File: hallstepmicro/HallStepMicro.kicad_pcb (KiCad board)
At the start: 2 copper layers, 30.5 x 55.9 mm, 26 parts, among them IC1 ATTINY84A-SS

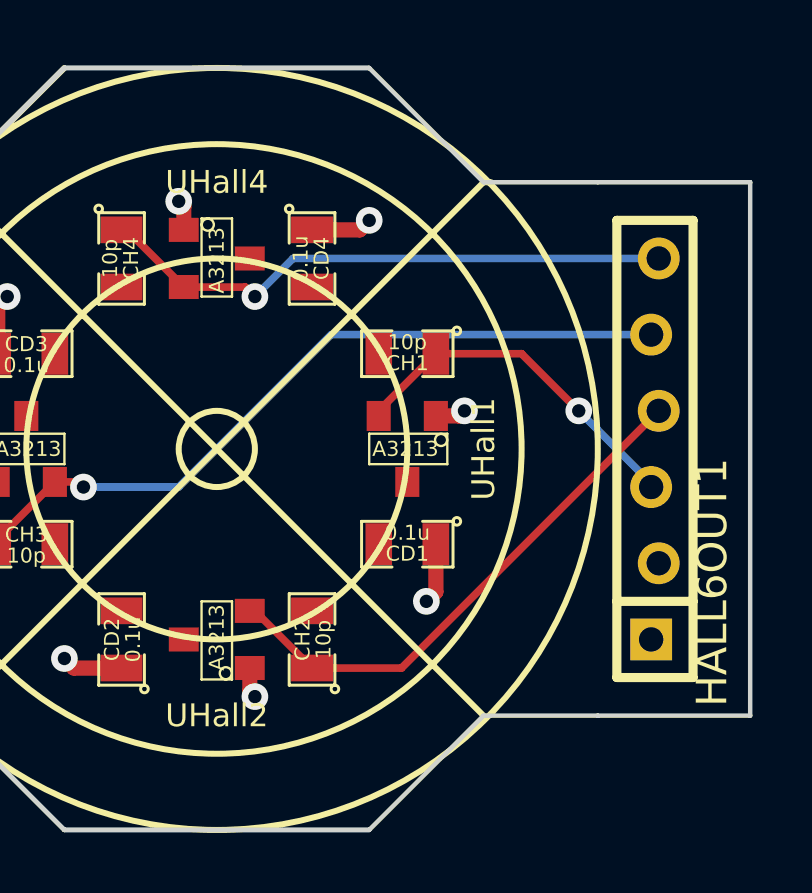
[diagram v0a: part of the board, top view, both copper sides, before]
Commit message: Shrinking sensor mount
Shrinking sensor mount dimensions. Intermediate checkin before
repositioning connector.
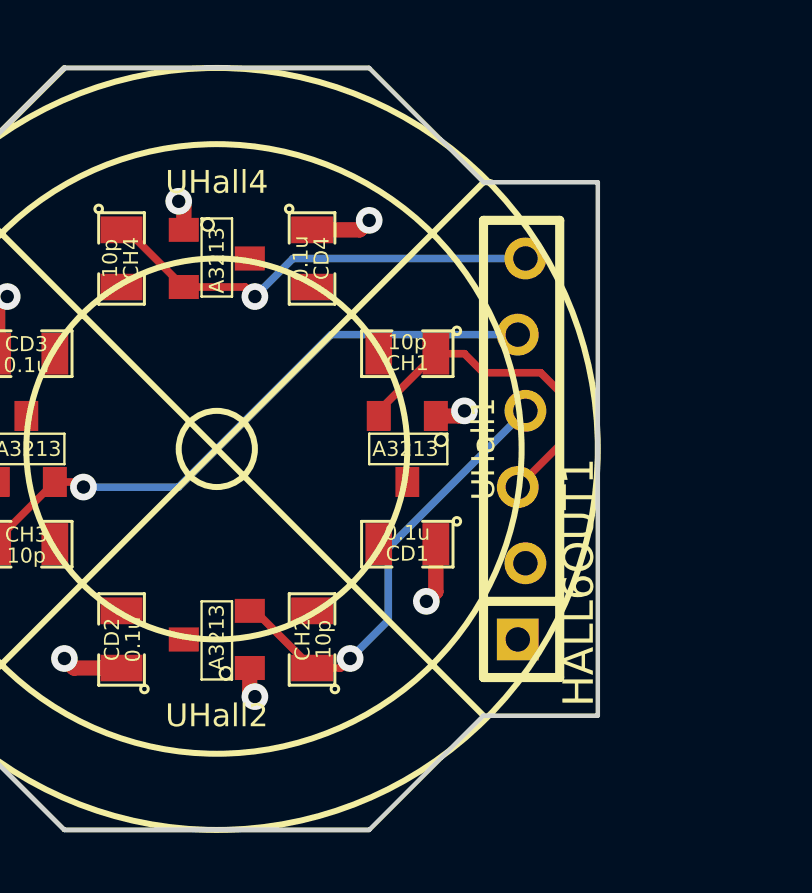
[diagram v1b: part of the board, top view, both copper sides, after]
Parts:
- moved HALL6OUT1 4.44 mm to (137.2, 76.2)
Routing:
- net /HallSensors1/hall3: track 24.9 -> 20.5 mm
- net /HallSensors1/hall4: track 19.7 -> 15.3 mm
- net /HallSensors1/hall2: track 18.0 -> 14.9 mm, vias 0 -> 1
- net /HallSensors1/hall1: track 12.0 -> 11.3 mm, vias 1 -> 0
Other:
- board size 30.5 x 55.9 mm -> 25.4 x 55.9 mm
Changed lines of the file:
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@@
-(kicad_pcb (version 3) (host pcbnew "(2013-mar-25)-stable")
+(kicad_pcb (version 3) (host pcbnew "(2013-07-07 BZR 4022)-stable")
   (general
     (links 70)
     (no_connects 0)
-    (area 101.229524 26.500001 144.855001 94.075)
+    (area 103.769524 26.500001 144.855001 94.075)
     (thickness 1.6)
-    (drawings 36)
-    (tracks 146)
+    (drawings 34)
+    (tracks 151)
     (zones 0)
     (modules 26)
@@
       (usegerberextensions true)
       (excludeedgelayer true)
-      (linewidth 0)
+      (linewidth 0.150000)
       (plotframeref false)
       (viasonmask false)
@@
   )
   (module SIL6-offset-0p005 (layer F.Cu)
-    (at 141.605 76.2 90)
+    (at 137.16 76.2 90)
     (descr "Connecteur 6 pins")
     (tags "CONN DEV")
@@
     )
   )
+  (gr_line (start 139.7 67.31) (end 139.7 85.09) (angle 90) (layer Edge.Cuts) (width 0.15))
   (gr_line (start 114.3 33.02) (end 139.7 33.02) (angle 90) (layer Edge.Cuts) (width 0.15))
   (gr_line (start 139.7 58.42) (end 114.3 58.42) (angle 90) (layer Edge.Cuts) (width 0.15))
@@
     (arrow2b (pts (xy 108.585 58.42) (xy 107.99858 57.293497)))
   )
-  (gr_line (start 144.78 67.31) (end 139.7 67.31) (angle 90) (layer Edge.Cuts) (width 0.15))
-  (gr_line (start 144.78 85.09) (end 144.78 67.31) (angle 90) (layer Edge.Cuts) (width 0.15))
-  (gr_line (start 139.7 85.09) (end 144.78 85.09) (angle 90) (layer Edge.Cuts) (width 0.15))
   (dimension 30.48 (width 0.25) (layer F.SilkS)
     (gr_text "1.2000 in" (at 129.54 93.074999) (layer F.SilkS)
@@
   (segment (start 133.6675 48.26) (end 133.6675 50.8) (width 0.254) (layer F.Cu) (net 4))
   (segment (start 133.6675 48.26) (end 135.89 48.26) (width 0.254) (layer F.Cu) (net 4))
-  (segment (start 134.3025 73.025) (end 137.16 73.025) (width 0.254) (layer F.Cu) (net 5))
-  (segment (start 141.478 77.343) (end 141.478 77.47) (width 0.254) (layer B.Cu) (net 5))
-  (segment (start 139.065 74.93) (end 141.478 77.343) (width 0.254) (layer B.Cu) (net 5))
-  (via (at 139.065 74.93) (size 0.889) (layers F.Cu B.Cu) (net 5))
-  (segment (start 137.16 73.025) (end 139.065 74.93) (width 0.254) (layer F.Cu) (net 5))
+  (segment (start 134.3025 73.025) (end 135.255 73.025) (width 0.254) (layer F.Cu) (net 5))
+  (segment (start 138.43 76.073) (end 137.033 77.47) (width 0.254) (layer F.Cu) (net 5))
+  (segment (start 138.43 74.295) (end 138.43 76.073) (width 0.254) (layer F.Cu) (net 5))
+  (segment (start 137.795 73.66) (end 138.43 74.295) (width 0.254) (layer F.Cu) (net 5))
+  (segment (start 135.89 73.66) (end 137.795 73.66) (width 0.254) (layer F.Cu) (net 5))
+  (segment (start 135.255 73.025) (end 135.89 73.66) (width 0.254) (layer F.Cu) (net 5))
   (segment (start 132.3975 75.10018) (end 132.3975 74.93) (width 0.254) (layer F.Cu) (net 5))
   (segment (start 132.3975 74.93) (end 134.3025 73.025) (width 0.254) (layer F.Cu) (net 5))
-  (segment (start 130.175 83.5025) (end 133.1595 83.5025) (width 0.254) (layer F.Cu) (net 6))
-  (segment (start 133.1595 83.5025) (end 141.732 74.93) (width 0.254) (layer F.Cu) (net 6))
+  (segment (start 130.175 83.5025) (end 131.1275 83.5025) (width 0.254) (layer F.Cu) (net 6))
+  (segment (start 132.715 79.502) (end 137.287 74.93) (width 0.254) (layer B.Cu) (net 6))
+  (segment (start 132.715 81.915) (end 132.715 79.502) (width 0.254) (layer B.Cu) (net 6))
+  (segment (start 131.445 83.185) (end 132.715 81.915) (width 0.254) (layer B.Cu) (net 6))
+  (via (at 131.445 83.185) (size 0.889) (layers F.Cu B.Cu) (net 6))
+  (segment (start 131.1275 83.5025) (end 131.445 83.185) (width 0.254) (layer F.Cu) (net 6))
   (segment (start 128.09982 81.5975) (end 128.27 81.5975) (width 0.254) (layer F.Cu) (net 6))
   (segment (start 128.27 81.5975) (end 130.175 83.5025) (width 0.254) (layer F.Cu) (net 6))
-  (segment (start 141.478 72.39) (end 130.81 72.39) (width 0.254) (layer B.Cu) (net 7))
+  (segment (start 137.033 72.39) (end 130.81 72.39) (width 0.254) (layer B.Cu) (net 7))
   (segment (start 122.38482 77.29982) (end 121.6025 77.29982) (width 0.254) (layer F.Cu) (net 7))
   (segment (start 122.555 77.47) (end 122.38482 77.29982) (width 0.254) (layer F.Cu) (net 7))
@@
   (segment (start 119.6975 79.375) (end 119.6975 79.20482) (width 0.254) (layer F.Cu) (net 7))
   (segment (start 119.6975 79.20482) (end 121.6025 77.29982) (width 0.254) (layer F.Cu) (net 7))
-  (segment (start 125.90018 70.8025) (end 127.9525 70.8025) (width 0.254) (layer F.Cu) (net 8))
-  (segment (start 129.54 69.85) (end 141.732 69.85) (width 0.254) (layer B.Cu) (net 8))
+  (segment (start 137.287 69.85) (end 129.54 69.85) (width 0.254) (layer B.Cu) (net 8))
+  (segment (start 127.9525 70.8025) (end 125.90018 70.8025) (width 0.254) (layer F.Cu) (net 8))
   (segment (start 128.27 71.12) (end 129.54 69.85) (width 0.254) (layer B.Cu) (net 8))
   (via (at 128.27 71.12) (size 0.889) (layers F.Cu B.Cu) (net 8))
@@
     (polygon
       (pts
-        (xy 144.78 85.09) (xy 135.89 85.09) (xy 132.08 88.9) (xy 121.92 88.9) (xy 114.3 81.28)
-        (xy 114.3 71.12) (xy 121.92 63.5) (xy 132.08 63.5) (xy 135.89 67.31) (xy 144.78 67.31)
+        (xy 139.7 85.09) (xy 135.89 85.09) (xy 132.08 88.9) (xy 121.92 88.9) (xy 114.3 81.28)
+        (xy 114.3 71.12) (xy 121.92 63.5) (xy 132.08 63.5) (xy 135.89 67.31) (xy 139.7 67.31)
       )
     )
@@
     (polygon
       (pts
-        (xy 144.78 85.09) (xy 135.89 85.09) (xy 132.08 88.9) (xy 121.92 88.9) (xy 114.3 81.28)
-        (xy 114.3 71.12) (xy 121.92 63.5) (xy 132.08 63.5) (xy 135.89 67.31) (xy 144.78 67.31)
+        (xy 139.7 85.09) (xy 135.89 85.09) (xy 132.08 88.9) (xy 121.92 88.9) (xy 114.3 81.28)
+        (xy 114.3 71.12) (xy 121.92 63.5) (xy 132.08 63.5) (xy 135.89 67.31) (xy 139.7 67.31)
       )
     )

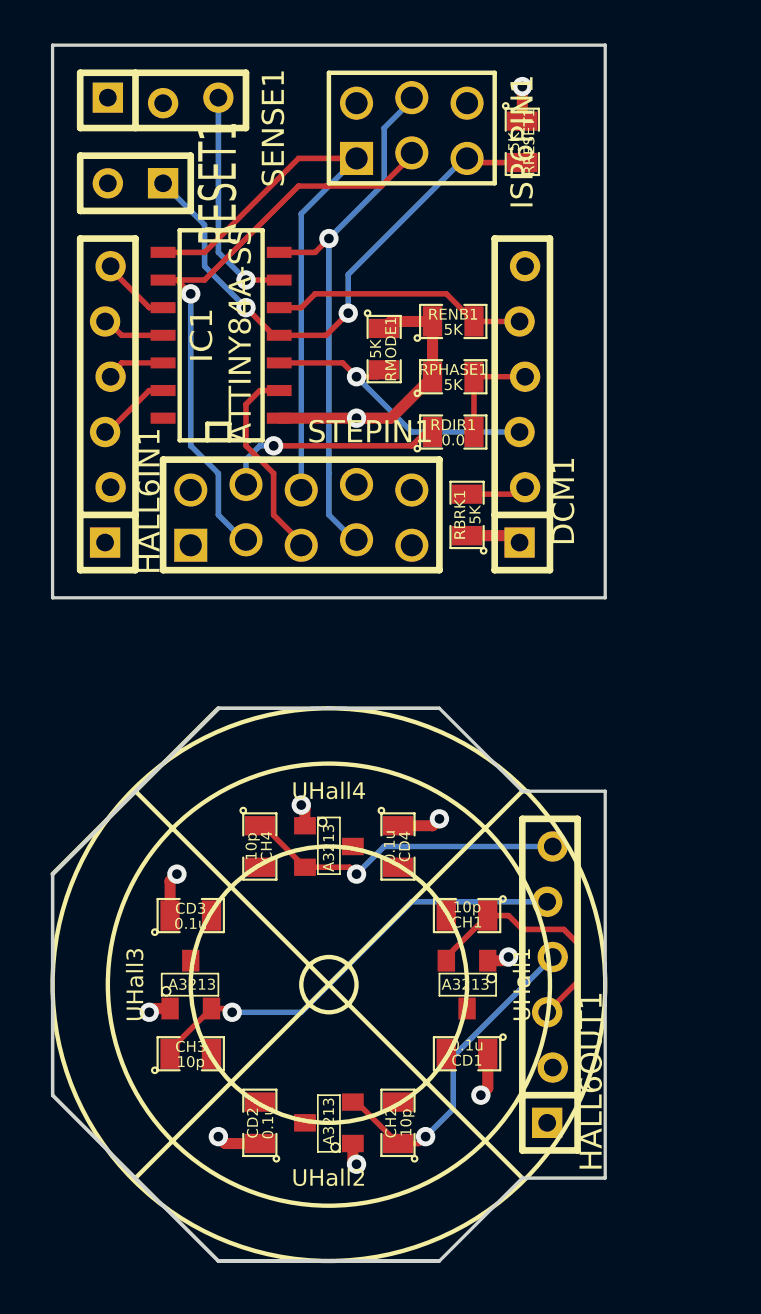
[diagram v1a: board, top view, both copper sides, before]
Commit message: Cleaned up routing.
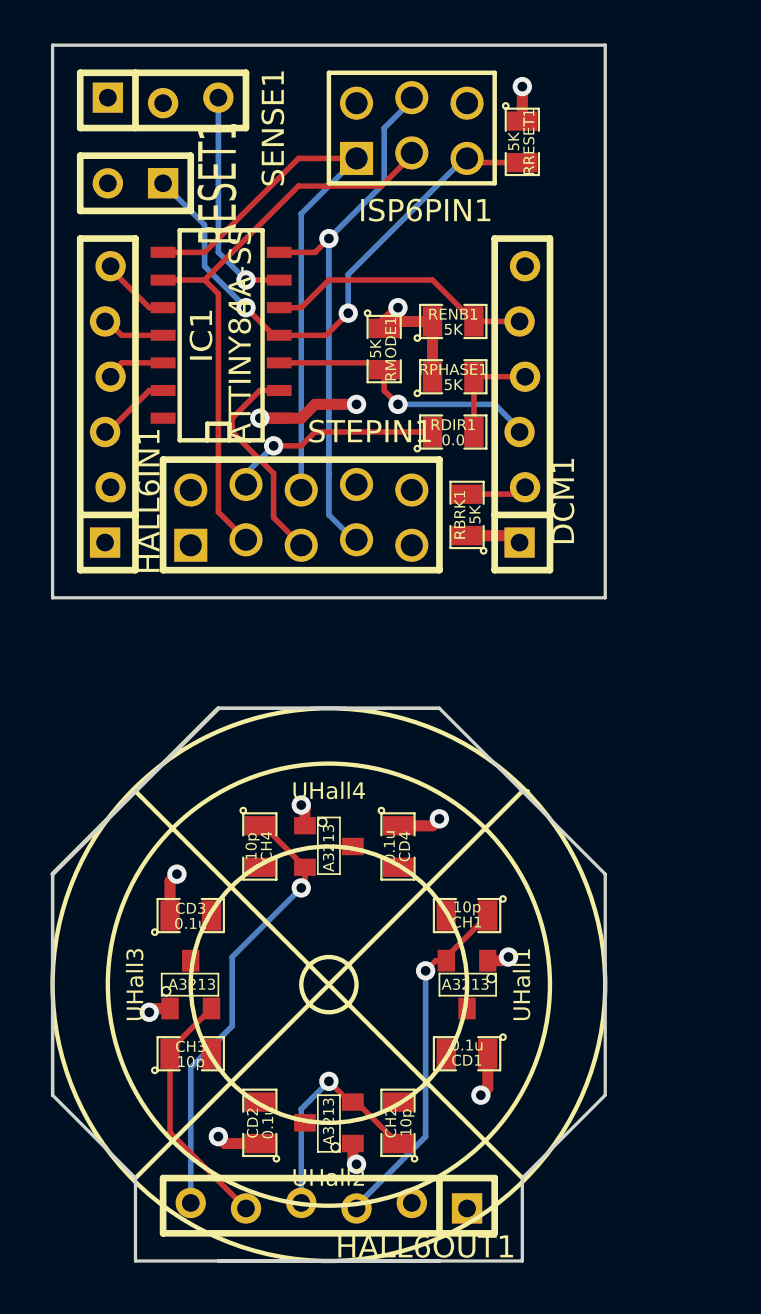
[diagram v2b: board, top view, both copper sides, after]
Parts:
- moved HALL6OUT1 14.4 mm to (127.0, 86.4), turned to 180 degrees
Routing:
- net /HallSensors1/hall3: track 20.5 -> 11.4 mm, vias 1 -> 0
- net /HallSensors1/hall4: track 15.3 -> 20.8 mm
- net /HallSensors1/hall1: track 11.3 -> 16.2 mm, vias 0 -> 1
- net /HallSensors1/hall2: track 14.9 -> 10.5 mm
- net VDD: track 17.0 -> 15.1 mm, vias 2 -> 4
- net /DC_MODE: track 14.5 -> 13.0 mm
- net /STP_STEP: track 27.8 -> 27.2 mm, vias 1 -> 0
- net /STP_ENB: track 9.19 -> 9.84 mm
- net /DC_ENABLE: track 12.0 -> 12.5 mm
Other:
- outline, holes or cut-outs redrawn

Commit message: Misc clean-up. Considered adding back TO92 case option but made design too cluttered.
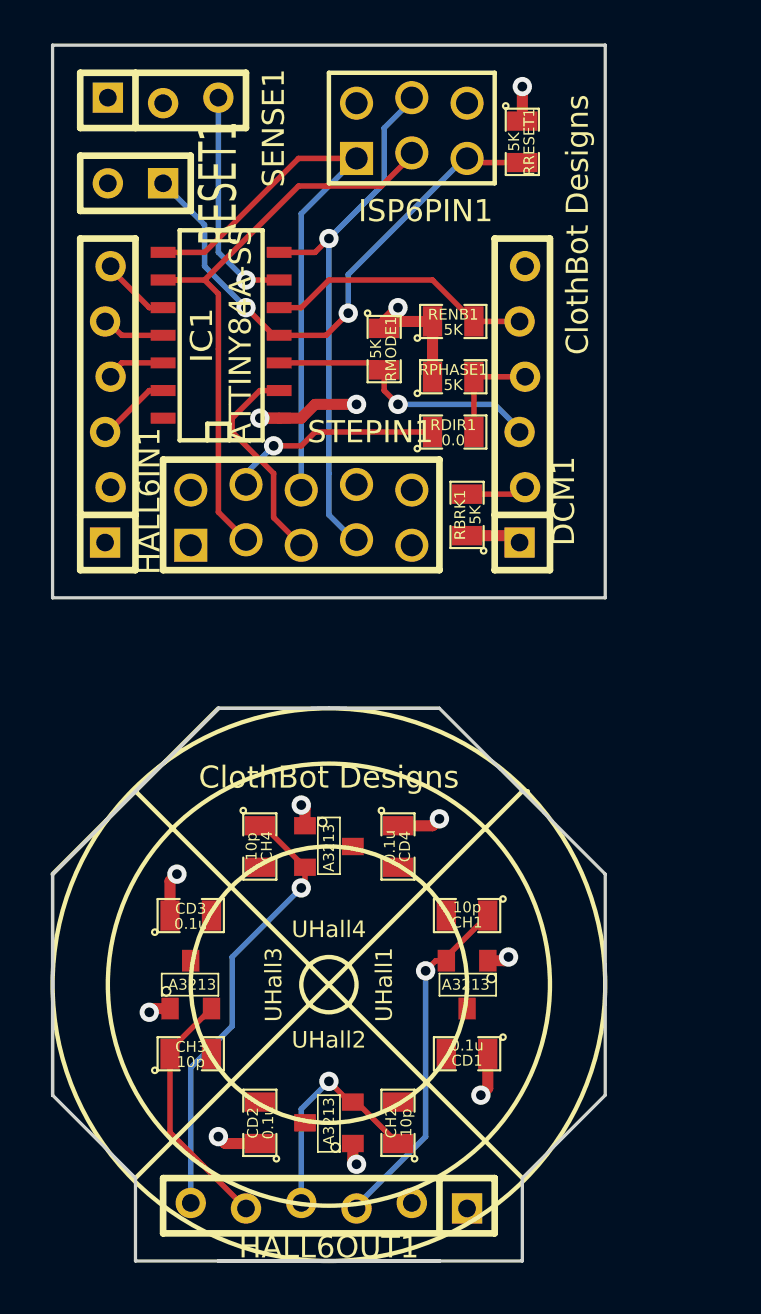
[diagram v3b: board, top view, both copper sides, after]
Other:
- board text added: "ClothBot Designs"
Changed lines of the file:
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@@
-(kicad_pcb (version 3) (host pcbnew "(2013-07-07 BZR 4022)-stable")
+(kicad_pcb (version 3) (host pcbnew "(2013-mar-25)-stable")
   (general
     (links 70)
     (no_connects 0)
-    (area 103.769524 26.500001 144.780001 94.075)
+    (area 98.171 26.500001 151.536401 100.736401)
     (thickness 1.6)
-    (drawings 35)
+    (drawings 33)
     (tracks 149)
     (zones 0)
@@
       (usegerberextensions true)
       (excludeedgelayer true)
-      (linewidth 0.150000)
+      (linewidth 0)
       (plotframeref false)
       (viasonmask false)
@@
       (effects (font (size 1.72974 1.08712) (thickness 0.3048)))
     )
-    (fp_text value CONN_2 (at 6.35 2.54 180) (layer F.SilkS) hide
+    (fp_text value CONN_2 (at 0 0 180) (layer F.SilkS) hide
       (effects (font (size 1.524 1.016) (thickness 0.3048)))
     )
@@
     (tags SOT23)
     (attr smd)
-    (fp_text reference UHall4 (at -2.54 0 360) (layer F.SilkS)
+    (fp_text reference UHall4 (at 3.81 0 360) (layer F.SilkS)
       (effects (font (size 0.762 0.762) (thickness 0.11938)))
     )
@@
     (tags SOT23)
     (attr smd)
-    (fp_text reference UHall3 (at -2.54 0 90) (layer F.SilkS)
+    (fp_text reference UHall3 (at 3.81 0 90) (layer F.SilkS)
       (effects (font (size 0.762 0.762) (thickness 0.11938)))
     )
@@
     (tags SOT23)
     (attr smd)
-    (fp_text reference UHall2 (at -2.54 0 180) (layer F.SilkS)
+    (fp_text reference UHall2 (at 3.81 0 180) (layer F.SilkS)
       (effects (font (size 0.762 0.762) (thickness 0.11938)))
     )
@@
     (tags SOT23)
     (attr smd)
-    (fp_text reference UHall1 (at -2.54 0 270) (layer F.SilkS)
+    (fp_text reference UHall1 (at 3.81 0 270) (layer F.SilkS)
       (effects (font (size 0.762 0.762) (thickness 0.11938)))
     )
@@
     (descr "Connecteur 6 pins")
     (tags "CONN DEV")
-    (fp_text reference HALL6OUT1 (at -4.445 -1.905 180) (layer F.SilkS)
-      (effects (font (size 1.016 1.016) (thickness 0.2032)))
-    )
-    (fp_text value CONN_6 (at 5.08 -2.54 180) (layer F.SilkS) hide
+    (fp_text reference HALL6OUT1 (at 0 -1.905 180) (layer F.SilkS)
+      (effects (font (size 1.016 1.016) (thickness 0.2032)))
+    )
+    (fp_text value CONN_6 (at 3.81 0 180) (layer F.SilkS) hide
       (effects (font (size 1.016 1.016) (thickness 0.2032)))
     )
@@
       (effects (font (size 1.016 1.016) (thickness 0.2032)))
     )
-    (fp_text value CONN_6 (at 5.08 -2.54 90) (layer F.SilkS) hide
+    (fp_text value CONN_6 (at 5.08 -1.27 90) (layer F.SilkS) hide
       (effects (font (size 1.016 1.016) (thickness 0.2032)))
     )
@@
       (effects (font (size 1.016 1.016) (thickness 0.2032)))
     )
-    (fp_text value CONN_3 (at 0 -1.905) (layer F.SilkS) hide
+    (fp_text value CONN_3 (at 0 0) (layer F.SilkS) hide
       (effects (font (size 1.016 1.016) (thickness 0.2032)))
     )
@@
       (effects (font (size 1.016 1.016) (thickness 0.2032)))
     )
-    (fp_text value CONN_5X2 (at -3.81 3.81) (layer F.SilkS) hide
+    (fp_text value CONN_5X2 (at -1.27 0) (layer F.SilkS) hide
       (effects (font (size 1.016 1.016) (thickness 0.2032)))
     )
@@
     )
   )
-  (dimension 25.4 (width 0.25) (layer F.SilkS)
-    (gr_text "1.0000 in" (at 127 92.439999) (layer F.SilkS)
-      (effects (font (size 1 1) (thickness 0.25)))
-    )
-    (feature1 (pts (xy 139.7 76.2) (xy 139.7 93.439999)))
-    (feature2 (pts (xy 114.3 76.2) (xy 114.3 93.439999)))
-    (crossbar (pts (xy 114.3 91.439999) (xy 139.7 91.439999)))
-    (arrow1a (pts (xy 139.7 91.439999) (xy 138.573497 92.026419)))
-    (arrow1b (pts (xy 139.7 91.439999) (xy 138.573497 90.853579)))
-    (arrow2a (pts (xy 114.3 91.439999) (xy 115.426503 92.026419)))
-    (arrow2b (pts (xy 114.3 91.439999) (xy 115.426503 90.853579)))
+  (gr_text "ClothBot Designs" (at 138.43 41.275 90) (layer F.SilkS)
+    (effects (font (size 1.016 1.016) (thickness 0.2032)))
+  )
+  (gr_text "ClothBot Designs" (at 127 66.675) (layer F.SilkS)
+    (effects (font (size 1.016 1.016) (thickness 0.2032)))
   )
   (gr_line (start 114.3 81.28) (end 118.11 85.09) (angle 90) (layer Edge.Cuts) (width 0.15))
@@
   (gr_line (start 139.7 58.42) (end 114.3 58.42) (angle 90) (layer Edge.Cuts) (width 0.15))
   (gr_line (start 139.7 33.02) (end 139.7 58.42) (angle 90) (layer Edge.Cuts) (width 0.15))
-  (dimension 25.4 (width 0.25) (layer F.SilkS)
-    (gr_text "1.0000 in" (at 127 27.575001) (layer F.SilkS)
-      (effects (font (size 1 1) (thickness 0.25)))
-    )
-    (feature1 (pts (xy 139.7 33.02) (xy 139.7 26.575001)))
-    (feature2 (pts (xy 114.3 33.02) (xy 114.3 26.575001)))
-    (crossbar (pts (xy 114.3 28.575001) (xy 139.7 28.575001)))
-    (arrow1a (pts (xy 139.7 28.575001) (xy 138.573497 29.161421)))
-    (arrow1b (pts (xy 139.7 28.575001) (xy 138.573497 27.988581)))
-    (arrow2a (pts (xy 114.3 28.575001) (xy 115.426503 29.161421)))
-    (arrow2b (pts (xy 114.3 28.575001) (xy 115.426503 27.988581)))
-  )
-  (dimension 25.4 (width 0.25) (layer F.SilkS)
-    (gr_text "1.0000 in" (at 107.585 45.72 90) (layer F.SilkS)
-      (effects (font (size 1 1) (thickness 0.25)))
-    )
-    (feature1 (pts (xy 114.3 33.02) (xy 106.585 33.02)))
-    (feature2 (pts (xy 114.3 58.42) (xy 106.585 58.42)))
-    (crossbar (pts (xy 108.585 58.42) (xy 108.585 33.02)))
-    (arrow1a (pts (xy 108.585 33.02) (xy 109.17142 34.146503)))
-    (arrow1b (pts (xy 108.585 33.02) (xy 107.99858 34.146503)))
-    (arrow2a (pts (xy 108.585 58.42) (xy 109.17142 57.293497)))
-    (arrow2b (pts (xy 108.585 58.42) (xy 107.99858 57.293497)))
-  )
-  (dimension 25.4 (width 0.25) (layer F.SilkS)
-    (gr_text "1.0000 in" (at 110.506 76.2 90) (layer F.SilkS)
-      (effects (font (size 1 1) (thickness 0.25)))
-    )
-    (feature1 (pts (xy 121.92 63.5) (xy 109.506 63.5)))
-    (feature2 (pts (xy 121.92 88.9) (xy 109.506 88.9)))
-    (crossbar (pts (xy 111.506 88.9) (xy 111.506 63.5)))
-    (arrow1a (pts (xy 111.506 63.5) (xy 112.09242 64.626503)))
-    (arrow1b (pts (xy 111.506 63.5) (xy 110.91958 64.626503)))
-    (arrow2a (pts (xy 111.506 88.9) (xy 112.09242 87.773497)))
-    (arrow2b (pts (xy 111.506 88.9) (xy 110.91958 87.773497)))
-  )
   (gr_line (start 114.3 58.42) (end 114.3 33.02) (angle 90) (layer Edge.Cuts) (width 0.15))
   (gr_line (start 121.92 88.9) (end 132.08 88.9) (angle 90) (layer Edge.Cuts) (width 0.15))
